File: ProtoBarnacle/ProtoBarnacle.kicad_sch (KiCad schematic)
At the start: 14 parts, among them J1 Conn_01x30, J11 Conn_02x35_JumperluxCardEdge, J12 Conn_02x35_JumperluxCardEdge, J2 Conn_01x30

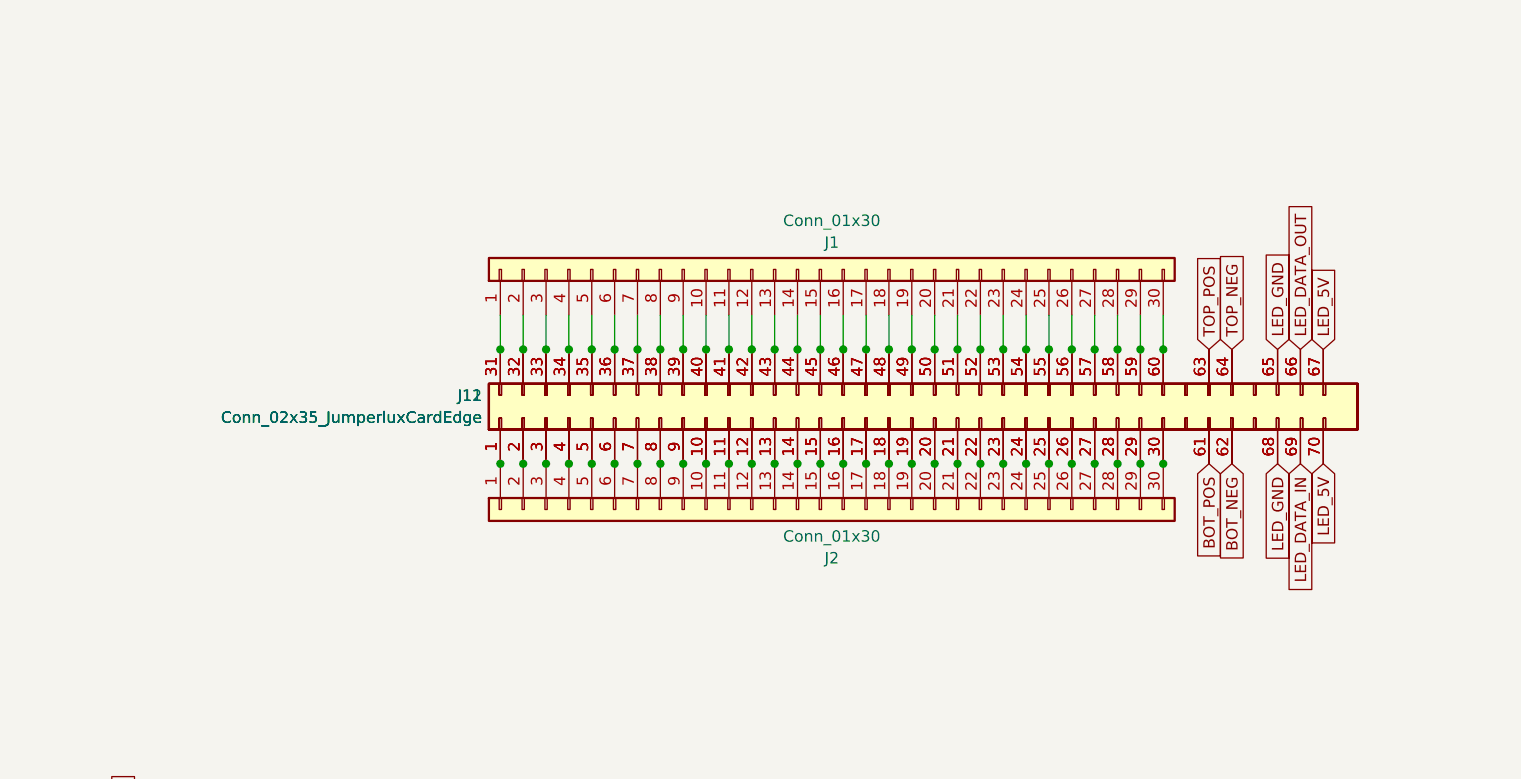
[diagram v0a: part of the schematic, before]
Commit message: Added silkscreen
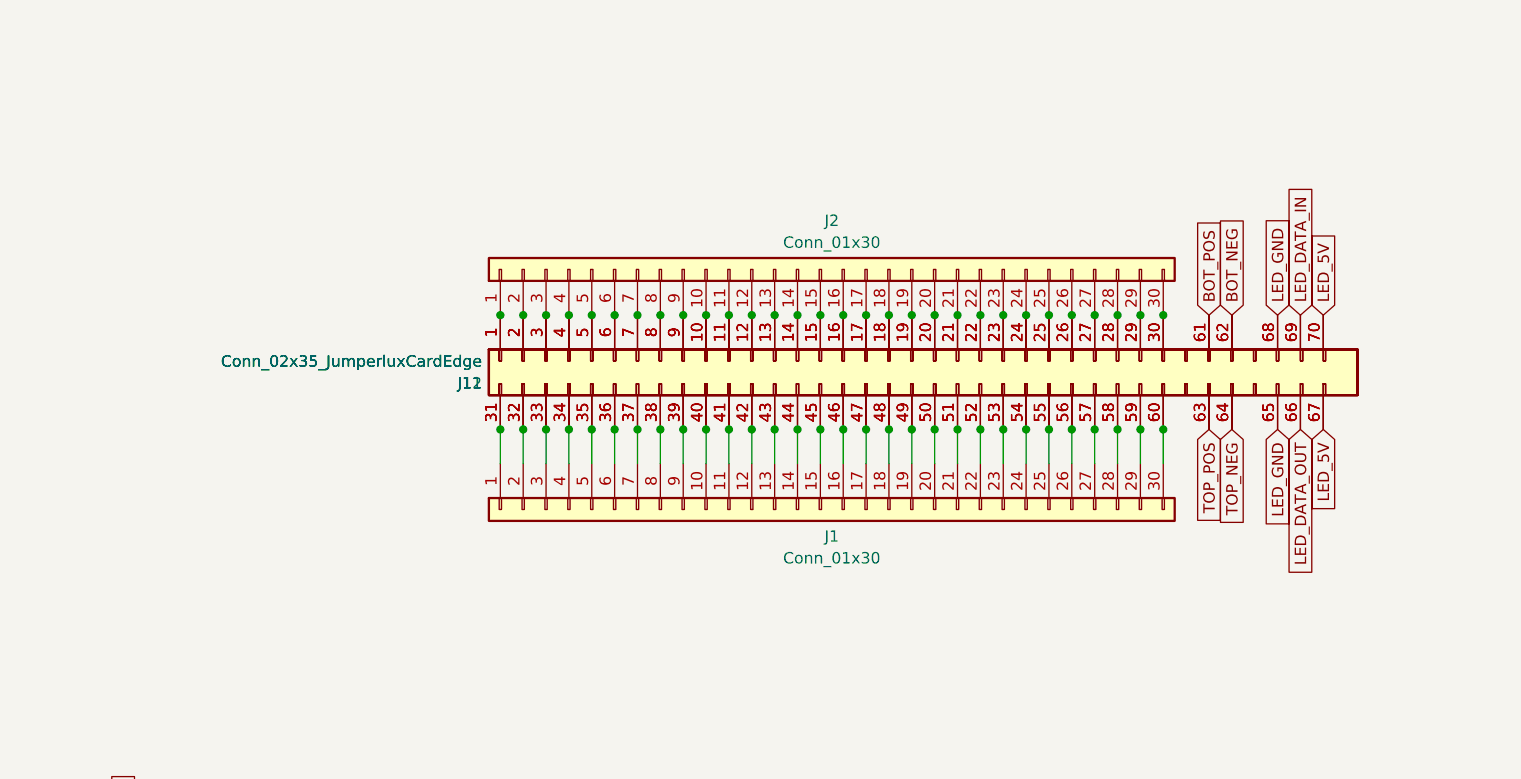
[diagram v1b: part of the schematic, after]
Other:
- moved on the sheet: J1, J11, J12, J2
